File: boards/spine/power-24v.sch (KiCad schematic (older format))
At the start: 9 parts, among them CON1 5-24V 5A, CON2 5-24V 16A, Q4 AOD4189

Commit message: BOM cleanup
Especially fix the confusing and mostly incorrect Mfg/Mfr stuff that I inherited from somewhere.
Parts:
- C72: Mfg1 (none) -> Murata; Mfg1Id (none) -> GRM21BR71H104MA01L; MfgId GRM21BR71H104MA01L -> (none); MfrId Murata -> (none)
- C73: Mfg1 (none) -> Murata; Mfg1Id (none) -> GRM219R61H105KA73D; MfgId GRM219R61H105KA73D -> (none); MfrId Murata -> (none)
- CON1: Mfg1 (none) -> Wurth; Mfg1Id (none) -> 694108105102; MfgId 694108105102 -> (none); MfrId Wurth -> (none)
- CON2: Mfg1 (none) -> E-xun; Mfg1Id (none) -> 2EDG-3.81; MfgId 2EDG-3.81 -> (none); MfrId E-xun -> (none)
- D8: Mfg1 (none) -> ON Semi; Mfg1Id (none) -> MMBZ12VALT1G; MfgId MMBZ12VALT1G -> (none); MfrId ON Semi -> (none)
- FB8, FB9: Mfg1 (none) -> Samsung; Mfg1Id (none) -> CIS21P300NE; MfgId CIS21P300NE -> (none); MfrId Samsung -> (none)
- Q4: Mfg1 (none) -> Alpha & Omega; Mfg1Id (none) -> AOD4189; MfgId Alpha & Omega -> (none); MfrId AOD4189 -> (none)
- R33: Mfg1 (none) -> Stackpole; Mfg1Id (none) -> RMCF0805JT100K; MfgId RMCF0805JT100K -> (none); MfrId Stackpole -> (none)
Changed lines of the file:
@@
 F 2 "Capacitors_SMD:C_0805" H 6888 4000 30  0001 C CNN
 F 3 "http://www.murata.com/~/media/webrenewal/support/library/catalog/products/capacitor/mlcc/c02e.ashx" H 6850 4150 60  0001 C CNN
-F 4 "GRM219R61H105KA73D" H 6900 3950 39  0001 L BNN "MfgId"
-F 5 "Murata" H 6850 4150 60  0001 C CNN "MfrId"
+F 4 "GRM219R61H105KA73D" H 6900 3950 39  0001 L BNN "Mfg1Id"
+F 5 "Murata" H 6850 4150 60  0001 C CNN "Mfg1"
 F 6 "Digikey" H 6850 4150 60  0001 C CNN "Vend1"
 F 7 "490-10743-2-ND" H 6850 4150 60  0001 C CNN "Vend1Id"
@@
 F 4 "Digikey" H 3250 4350 60  0001 C CNN "Vend1"
 F 5 "732-5932-1-ND" H 3250 4350 60  0001 C CNN "Vend1Id"
-F 6 "Wurth" H 3250 4350 60  0001 C CNN "MfrId"
-F 7 "694108105102" H 3250 4350 60  0001 C CNN "MfgId"
+F 6 "Wurth" H 3250 4350 60  0001 C CNN "Mfg1"
+F 7 "694108105102" H 3250 4350 60  0001 C CNN "Mfg1Id"
 F 8 "1.13" H 3250 4350 60  0001 C CNN "RefPrice1k"
 	1    3250 4350
@@
 F 4 "Digikey" H 5350 3800 60  0001 C CNN "Vend1"
 F 5 "785-1351-1-ND" H 5350 3800 60  0001 C CNN "Vend1Id"
-F 6 "Alpha & Omega" H 5350 3800 60  0001 C CNN "MfgId"
-F 7 "AOD4189" H 5350 3800 60  0001 C CNN "MfrId"
+F 6 "Alpha & Omega" H 5350 3800 60  0001 C CNN "Mfg1"
+F 7 "AOD4189" H 5350 3800 60  0001 C CNN "Mfg1Id"
 F 8 "0.196" H 5350 3800 60  0001 C CNN "RefPrice1k"
 	1    5350 3800
@@
 F 5 "490-9672-2-ND" V 5000 4400 60  0001 C CNN "Vend1Id"
 F 6 "Digikey" V 5000 4400 60  0001 C CNN "Vend1"
-F 7 "Murata" V 5000 4400 60  0001 C CNN "MfrId"
-F 8 "GRM21BR71H104MA01L" V 5000 4400 60  0001 C CNN "MfgId"
+F 7 "Murata" V 5000 4400 60  0001 C CNN "Mfg1"
+F 8 "GRM21BR71H104MA01L" V 5000 4400 60  0001 C CNN "Mfg1Id"
 	1    5000 4400
 	-1   0    0    1
@@
 F 6 "0.23" H 4450 4400 60  0001 C CNN "RefPrice1k"
 F 7 "4way 4pin Screw PCB Terminal Block Connector 3.81mm Pitch Pluggable Type" H 4450 4400 60  0001 C CNN "Description"
-F 8 "E-xun" H 4450 4400 60  0001 C CNN "MfrId"
-F 9 "2EDG-3.81" H 4450 4400 60  0001 C CNN "MfgId"
+F 8 "E-xun" H 4450 4400 60  0001 C CNN "Mfg1"
+F 9 "2EDG-3.81" H 4450 4400 60  0001 C CNN "Mfg1Id"
 	1    4450 4400
 	1    0    0    -1
@@
 F 2 "TO_SOT_Packages_SMD:SOT-23" H 6100 4100 60  0001 C CNN
 F 3 "http://www.onsemi.com/pub_link/Collateral/MMBZ5V6ALT1-D.PDF" H 6100 4100 60  0001 C CNN
-F 4 "ON Semi" H 5750 4250 39  0001 L BNN "MfrId"
-F 5 "MMBZ12VALT1G" H 6100 4200 39  0000 C CNN "MfgId"
+F 4 "ON Semi" H 5750 4250 39  0001 L BNN "Mfg1"
+F 5 "MMBZ12VALT1G" H 6100 4200 39  0000 C CNN "Mfg1Id"
 F 6 "MMBZ12VALT1GOSCT-ND" H 6100 4100 60  0001 C CNN "Vend1Id"
 F 7 ".04471" H 6100 4100 60  0001 C CNN "RefPrice1k"
@@
 F 3 "https://www.seielect.com/Catalog/SEI-RMCF_RMCP.pdf" H 5350 4700 30  0001 C CNN
 F 4 "Digikey" V 5350 4700 60  0001 C CNN "Vend1"
-F 5 "Stackpole" V 5350 4700 60  0001 C CNN "MfrId"
-F 6 "RMCF0805JT100K" V 5350 4700 60  0001 C CNN "MfgId"
+F 5 "Stackpole" V 5350 4700 60  0001 C CNN "Mfg1"
+F 6 "RMCF0805JT100K" V 5350 4700 60  0001 C CNN "Mfg1Id"
 F 7 "RMCF0805JT100KCT-ND" V 5350 4700 60  0001 C CNN "Vend1Id"
 F 8 "0.00320" V 5350 4700 60  0001 C CNN "RefPrice1k"
@@
 F 3 "http://www.samsungsem.com/kr/front/downloadcms.do?path=/kr/support/product-search/bead/__icsFiles/afieldfile/2014/11/13&fileName=S_CIS21J121NE.pdf" H 7125 4850 60  0001 C CNN
 F 4 "0.02383" H 7100 4850 60  0001 C CNN "RefPrice1k"
-F 5 "Samsung" H 7100 4850 60  0001 C CNN "MfrId"
-F 6 "CIS21P300NE" H 7100 4850 60  0001 C CNN "MfgId"
+F 5 "Samsung" H 7100 4850 60  0001 C CNN "Mfg1"
+F 6 "CIS21P300NE" H 7100 4850 60  0001 C CNN "Mfg1Id"
 F 7 "Digikey" H 7100 4850 60  0001 C CNN "Vend1"
 F 8 "1276-6370-1-ND" H 7100 4850 60  0001 C CNN "Vend1Id"
@@
 FB 59 00 E6 A5 69 3A 37 9E CF 73 BC F7 37 E3 33 5D 9E A8 3E 7F 80 FA F7 F6 BB 44 F4 6E D4 E7 77
 A2 1E 1F 27 A2 E3 16 70 32 E9 54 FE 3F E7 AF 00 CA 1C A3 36 0A 00 00 00 00 49 45 4E 44 AE 42 60
-82 00
+82 70
 EndData
 $EndBitmap
@@
 F 3 "http://www.samsungsem.com/kr/front/downloadcms.do?path=/kr/support/product-search/bead/__icsFiles/afieldfile/2014/11/13&fileName=S_CIS21J121NE.pdf" H 7125 5150 60  0001 C CNN
 F 4 "0.02383" H 7100 5150 60  0001 C CNN "RefPrice1k"
-F 5 "Samsung" H 7100 5150 60  0001 C CNN "MfrId"
-F 6 "CIS21P300NE" H 7100 5150 60  0001 C CNN "MfgId"
+F 5 "Samsung" H 7100 5150 60  0001 C CNN "Mfg1"
+F 6 "CIS21P300NE" H 7100 5150 60  0001 C CNN "Mfg1Id"
 F 7 "Digikey" H 7100 5150 60  0001 C CNN "Vend1"
 F 8 "1276-6370-1-ND" H 7100 5150 60  0001 C CNN "Vend1Id"

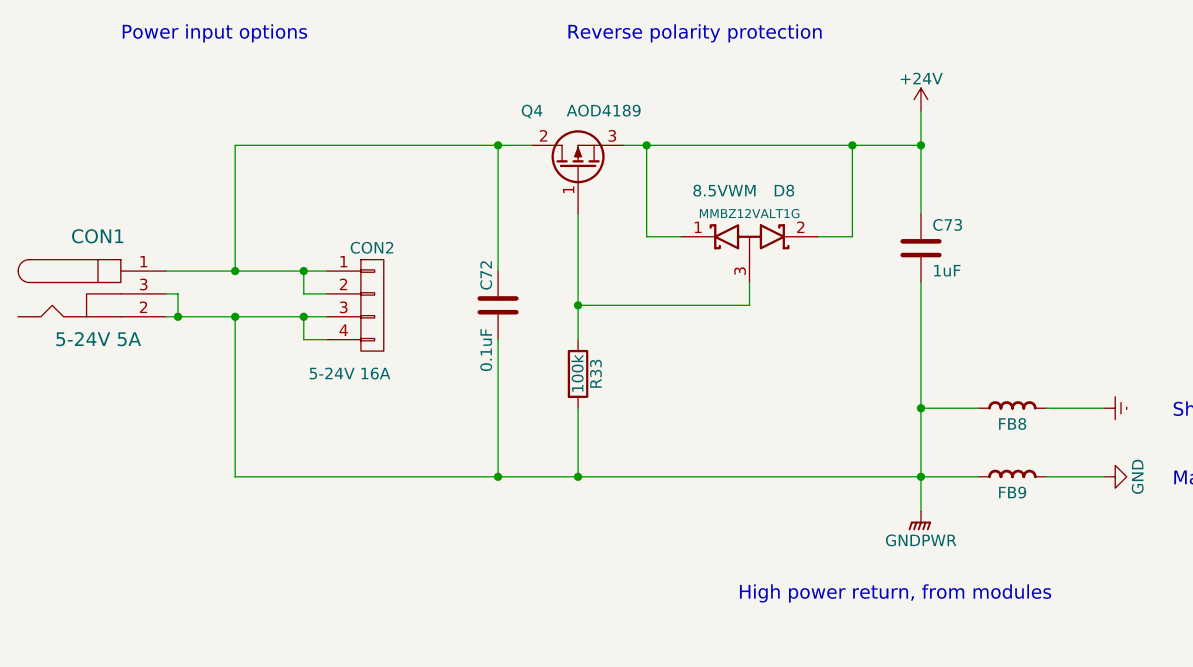
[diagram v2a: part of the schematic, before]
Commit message: Capacitor upgrades, BOM tidying
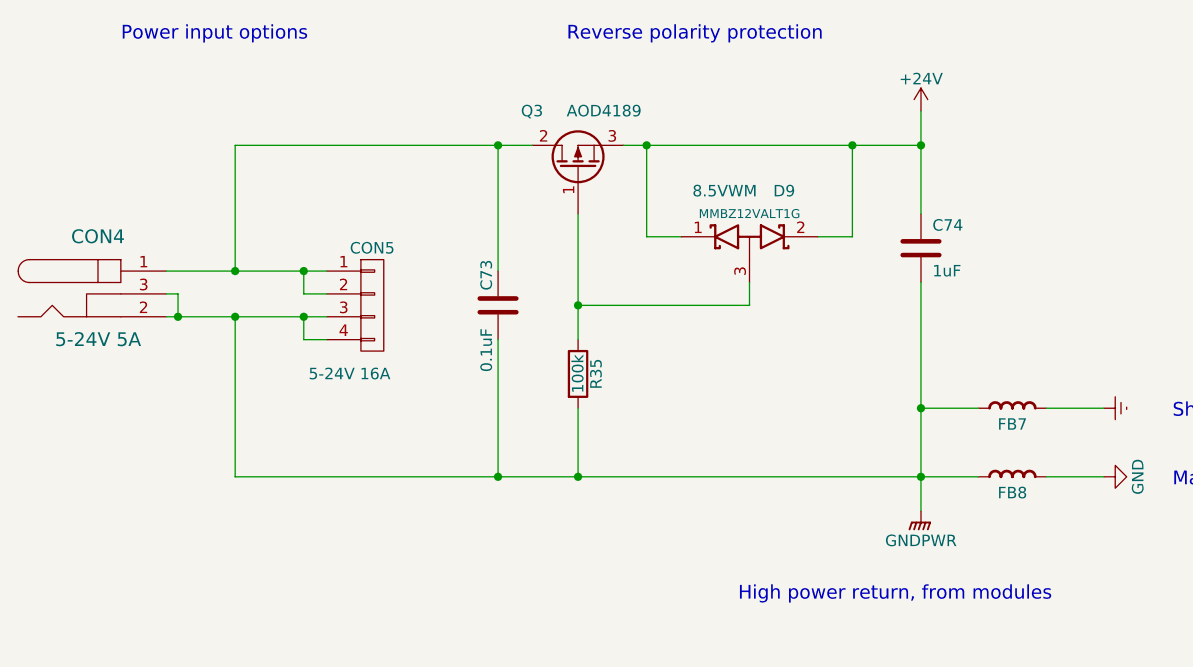
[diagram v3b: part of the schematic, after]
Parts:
- renumbered C72 to C73, C73 to C74, CON1 to CON4, CON2 to CON5, D8 to D9, FB8 to FB7, FB9 to FB8, Q4 to Q3, R33 to R35
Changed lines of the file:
@@
 $EndDescr
 $Comp
-L +24V #PWR0139
+L +24V #PWR149
 U 1 1 564D5D45
 P 6850 3550
-F 0 "#PWR0139" H 6850 3400 50  0001 C CNN
+F 0 "#PWR149" H 6850 3400 50  0001 C CNN
 F 1 "+24V" H 6850 3690 50  0000 C CNN
 F 2 "" H 6850 3550 60  0000 C CNN
@@
 $EndComp
 $Comp
-L GNDPWR #PWR0140
+L GNDPWR #PWR150
 U 1 1 564D5D5C
 P 6850 5300
-F 0 "#PWR0140" H 6850 5100 50  0001 C CNN
+F 0 "#PWR150" H 6850 5100 50  0001 C CNN
 F 1 "GNDPWR" H 6850 5170 50  0000 C CNN
 F 2 "" H 6850 5250 60  0000 C CNN
@@
 $EndComp
 $Comp
-L C C73
+L C C74
 U 1 1 564D690E
 P 6850 4150
-F 0 "C73" H 6900 4250 50  0000 L CNN
+F 0 "C74" H 6900 4250 50  0000 L CNN
 F 1 "1uF " H 6900 4050 50  0000 L CNN
 F 2 "Capacitors_SMD:C_0805" H 6888 4000 30  0001 C CNN
@@
 $EndComp
 $Comp
-L GND #PWR0141
+L GND #PWR152
 U 1 1 564D690F
 P 7650 5150
-F 0 "#PWR0141" H 7650 4900 50  0001 C CNN
+F 0 "#PWR152" H 7650 4900 50  0001 C CNN
 F 1 "GND" H 7650 5000 50  0000 C CNN
 F 2 "" H 7650 5150 60  0000 C CNN
@@
 $EndComp
 $Comp
-L BARREL_JACK CON1
+L BARREL_JACK CON4
 U 1 1 564D6BF2
 P 3250 4350
-F 0 "CON1" H 3250 4600 60  0000 C CNN
+F 0 "CON4" H 3250 4600 60  0000 C CNN
 F 1 "5-24V 5A" H 3250 4150 60  0000 C CNN
 F 2 "Connect:BARREL_JACK" H 3250 4350 60  0001 C CNN
@@
 $EndComp
 $Comp
-L Q_PMOS_GDS Q4
+L Q_PMOS_GDS Q3
 U 1 1 564D73AF
 P 5350 3800
-F 0 "Q4" V 5600 4050 50  0000 R CNN
+F 0 "Q3" V 5600 4050 50  0000 R CNN
 F 1 "AOD4189" V 5600 3850 50  0000 R CNN
 F 2 "TO_SOT_Packages_SMD:TO-252-2Lead" H 5550 3900 29  0001 C CNN
@@
 	3850 3700 5150 3700
 $Comp
-L C C72
+L C C73
 U 1 1 564D7783
 P 5000 4400
-F 0 "C72" V 5050 4200 50  0000 L CNN
+F 0 "C73" V 5050 4200 50  0000 L CNN
 F 1 "0.1uF" V 5050 4500 50  0000 L CNN
 F 2 "Capacitors_SMD:C_0805" H 5038 4250 30  0001 C CNN
@@
 Connection ~ 5000 5150
 $Comp
-L CONN_01X04 CON2
+L CONN_01X04 CON5
 U 1 1 564D79D9
 P 4450 4400
-F 0 "CON2" H 4450 4650 50  0000 C CNN
+F 0 "CON5" H 4450 4650 50  0000 C CNN
 F 1 "5-24V 16A" H 4350 4100 50  0000 C CNN
 F 2 "Terminal_Blocks:TerminalBlock_Pheonix_PT-3.5mm_4pol" H 4450 4400 60  0001 C CNN
@@
 Power input options
 $Comp
-L D_Schottky_x2_ACom_KKA D8
+L D_Schottky_x2_ACom_KKA D9
 U 1 1 564D8C89
 P 6100 4100
-F 0 "D8" H 6300 4300 50  0000 R CNN
+F 0 "D9" H 6300 4300 50  0000 R CNN
 F 1 "8.5VWM" H 5850 4300 50  0000 L CNN
 F 2 "TO_SOT_Packages_SMD:SOT-23" H 6100 4100 60  0001 C CNN
@@
 $EndComp
 $Comp
-L R R33
+L R R35
 U 1 1 564DB940
 P 5350 4700
-F 0 "R33" V 5430 4700 50  0000 C CNN
+F 0 "R35" V 5430 4700 50  0000 C CNN
 F 1 "100k" V 5350 4700 50  0000 C CNN
 F 2 "Resistors_SMD:R_0805" V 5280 4700 30  0001 C CNN
@@
 Connection ~ 6850 5150
 $Comp
-L Earth #PWR0142
+L Earth #PWR151
 U 1 1 565B7572
 P 7650 4850
-F 0 "#PWR0142" H 7650 4600 50  0001 C CNN
+F 0 "#PWR151" H 7650 4600 50  0001 C CNN
 F 1 "Earth" H 7650 4700 50  0001 C CNN
 F 2 "" H 7650 4850 60  0000 C CNN
@@
 High power return, from modules
 $Comp
-L FERRITE_BEAD FB8
+L FERRITE_BEAD FB7
 U 1 1 565EA3EB
 P 7100 4850
-F 0 "FB8" H 7250 4750 50  0000 C BNN
+F 0 "FB7" H 7250 4750 50  0000 C BNN
 F 1 "Ferrite bead" H 7500 4750 39  0001 C BNN
 F 2 "Resistors_SMD:R_0805" H 7100 5000 50  0001 C CNN
@@
 FB 59 00 E6 A5 69 3A 37 9E CF 73 BC F7 37 E3 33 5D 9E A8 3E 7F 80 FA F7 F6 BB 44 F4 6E D4 E7 77
 A2 1E 1F 27 A2 E3 16 70 32 E9 54 FE 3F E7 AF 00 CA 1C A3 36 0A 00 00 00 00 49 45 4E 44 AE 42 60
-82 70
+82 00
 EndData
 $EndBitmap
@@
 72 0F 1C A9 DC 70 49 CB 79 33 88 85 99 AD 01 6C 4B 10 FC 3B 13 DE 3B 37 68 79 AD 07 BC 00 3C 0E
 3C 31 EE E3 D8 E7 0F 03 D7 7B 9F FB C1 E1 FF 01 18 C4 96 1D B8 0E 40 07 00 00 00 00 49 45 4E 44
-AE 42 60 82 00
+AE 42 60 82 10
 EndData
 $EndBitmap
@@
 Shield ground
 $Comp
-L FERRITE_BEAD FB9
+L FERRITE_BEAD FB8
 U 1 1 565EB470
 P 7100 5150
-F 0 "FB9" H 7250 5050 50  0000 C BNN
+F 0 "FB8" H 7250 5050 50  0000 C BNN
 F 1 "Ferrite bead" H 7500 5050 39  0001 C BNN
 F 2 "Resistors_SMD:R_0805" H 7100 5300 50  0001 C CNN

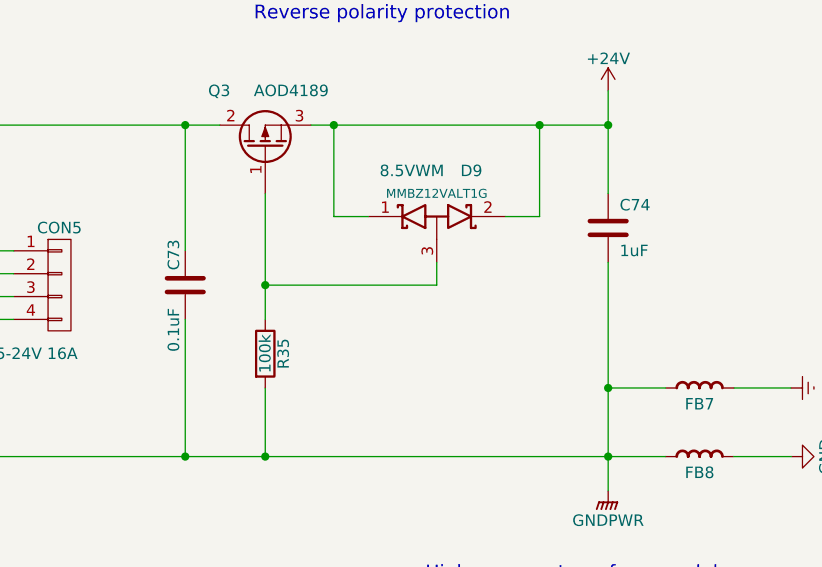
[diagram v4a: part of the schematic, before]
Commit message: Schematics stabilizing for next proto, starting PCB updates
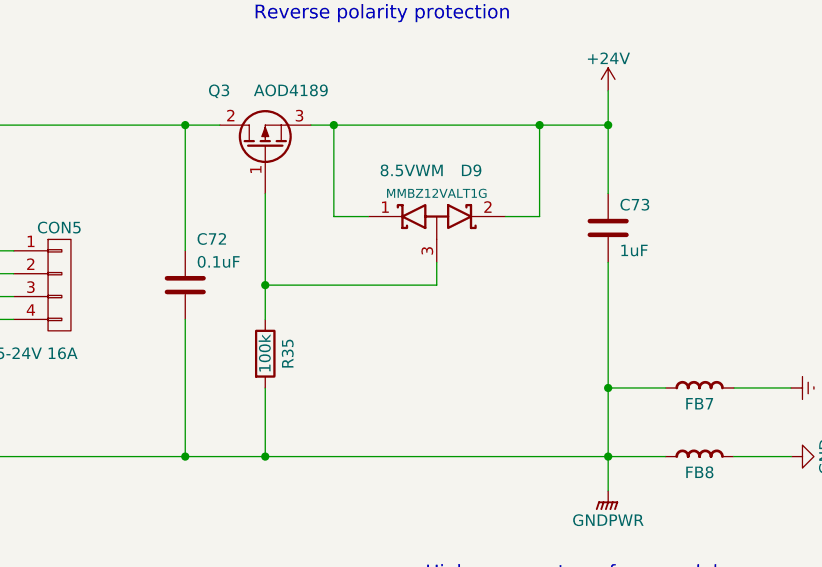
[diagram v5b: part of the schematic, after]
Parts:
- renumbered C73 to C72, C74 to C73
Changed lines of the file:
@@
 $EndComp
 $Comp
-L C C74
+L C C73
 U 1 1 564D690E
 P 6850 4150
-F 0 "C74" H 6900 4250 50  0000 L CNN
+F 0 "C73" H 6900 4250 50  0000 L CNN
 F 1 "1uF " H 6900 4050 50  0000 L CNN
 F 2 "Capacitors_SMD:C_0805" H 6888 4000 30  0001 C CNN
@@
 	3850 3700 5150 3700
 $Comp
-L C C73
+L C C72
 U 1 1 564D7783
 P 5000 4400
-F 0 "C73" V 5050 4200 50  0000 L CNN
-F 1 "0.1uF" V 5050 4500 50  0000 L CNN
+F 0 "C72" H 4950 4200 50  0000 R CNN
+F 1 "0.1uF" H 4950 4300 50  0000 R CNN
 F 2 "Capacitors_SMD:C_0805" H 5038 4250 30  0001 C CNN
 F 3 "http://psearch.murata.com/capacitor/product/GRM21BR71H104MA01%23.pdf" H 5000 4400 60  0001 C CNN
@@
 U 1 1 564DB940
 P 5350 4700
-F 0 "R35" V 5430 4700 50  0000 C CNN
+F 0 "R35" V 5450 4700 50  0000 C CNN
 F 1 "100k" V 5350 4700 50  0000 C CNN
 F 2 "Resistors_SMD:R_0805" V 5280 4700 30  0001 C CNN
@@
 72 0F 1C A9 DC 70 49 CB 79 33 88 85 99 AD 01 6C 4B 10 FC 3B 13 DE 3B 37 68 79 AD 07 BC 00 3C 0E
 3C 31 EE E3 D8 E7 0F 03 D7 7B 9F FB C1 E1 FF 01 18 C4 96 1D B8 0E 40 07 00 00 00 00 49 45 4E 44
-AE 42 60 82 01
+AE 42 60 82 00
 EndData
 $EndBitmap

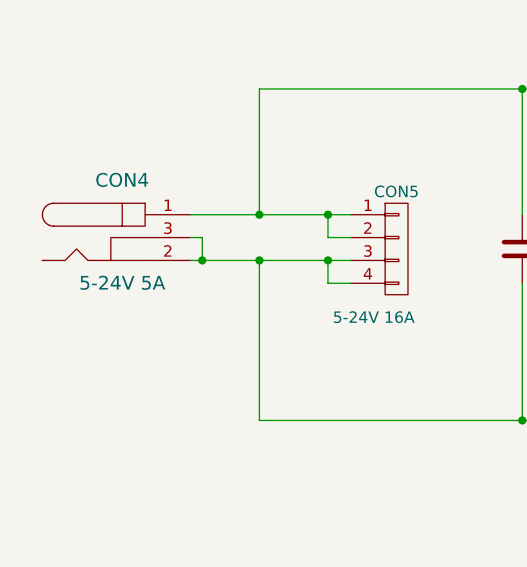
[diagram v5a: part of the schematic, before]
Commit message: Draft for new mechanical layout
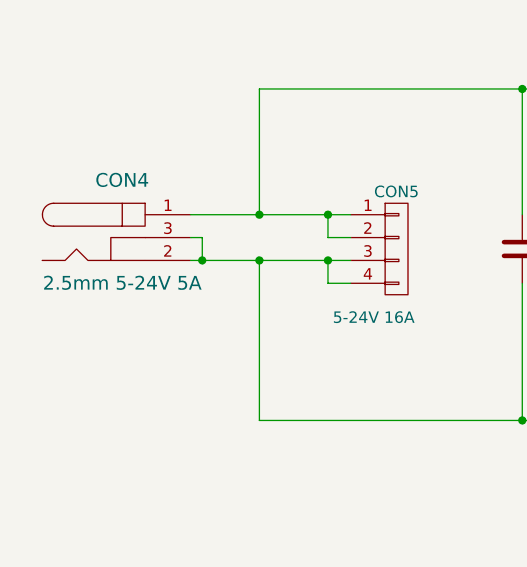
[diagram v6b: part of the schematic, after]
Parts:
- CON4: value 5-24V 5A -> 2.5mm 5-24V 5A
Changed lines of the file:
@@
 P 3250 4350
 F 0 "CON4" H 3250 4600 60  0000 C CNN
-F 1 "5-24V 5A" H 3250 4150 60  0000 C CNN
+F 1 "2.5mm 5-24V 5A" H 3250 4150 60  0000 C CNN
 F 2 "Connect:BARREL_JACK" H 3250 4350 60  0001 C CNN
 F 3 "http://katalog.we-online.de/em/datasheet/6941xx105102.pdf" H 3250 4350 60  0001 C CNN
